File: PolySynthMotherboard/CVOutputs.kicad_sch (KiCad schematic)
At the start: 167 parts, among them U301 DAC7578xPW, U302 TL074, U303 TL072, U304 TMUX4051, U305 TL074, U306 TMUX4051, U307 TL074, U308 TMUX4051, U309 TMUX4051, U310 TL074, U311 TL074, U312 TL074, U313 TMUX4051, U314 TL074, U315 TL074, U316 TL074, U317 TMUX4051, U318 TMUX4051, U319 TL074, U320 TL074

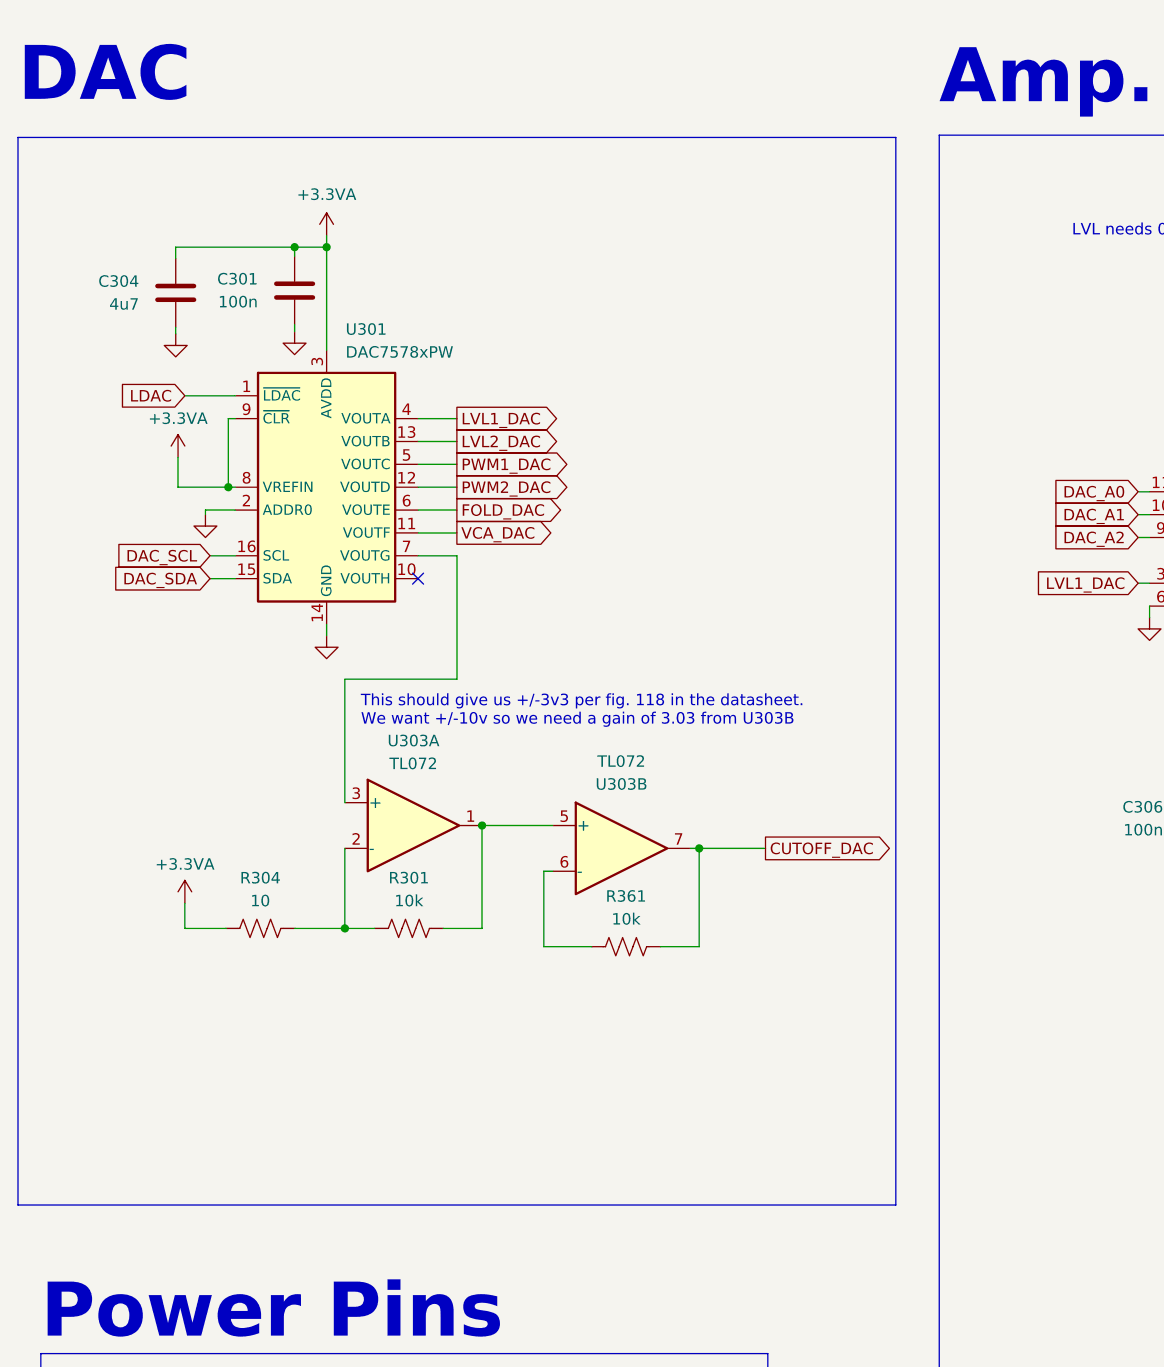
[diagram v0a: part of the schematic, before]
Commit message: DAC7578 driver
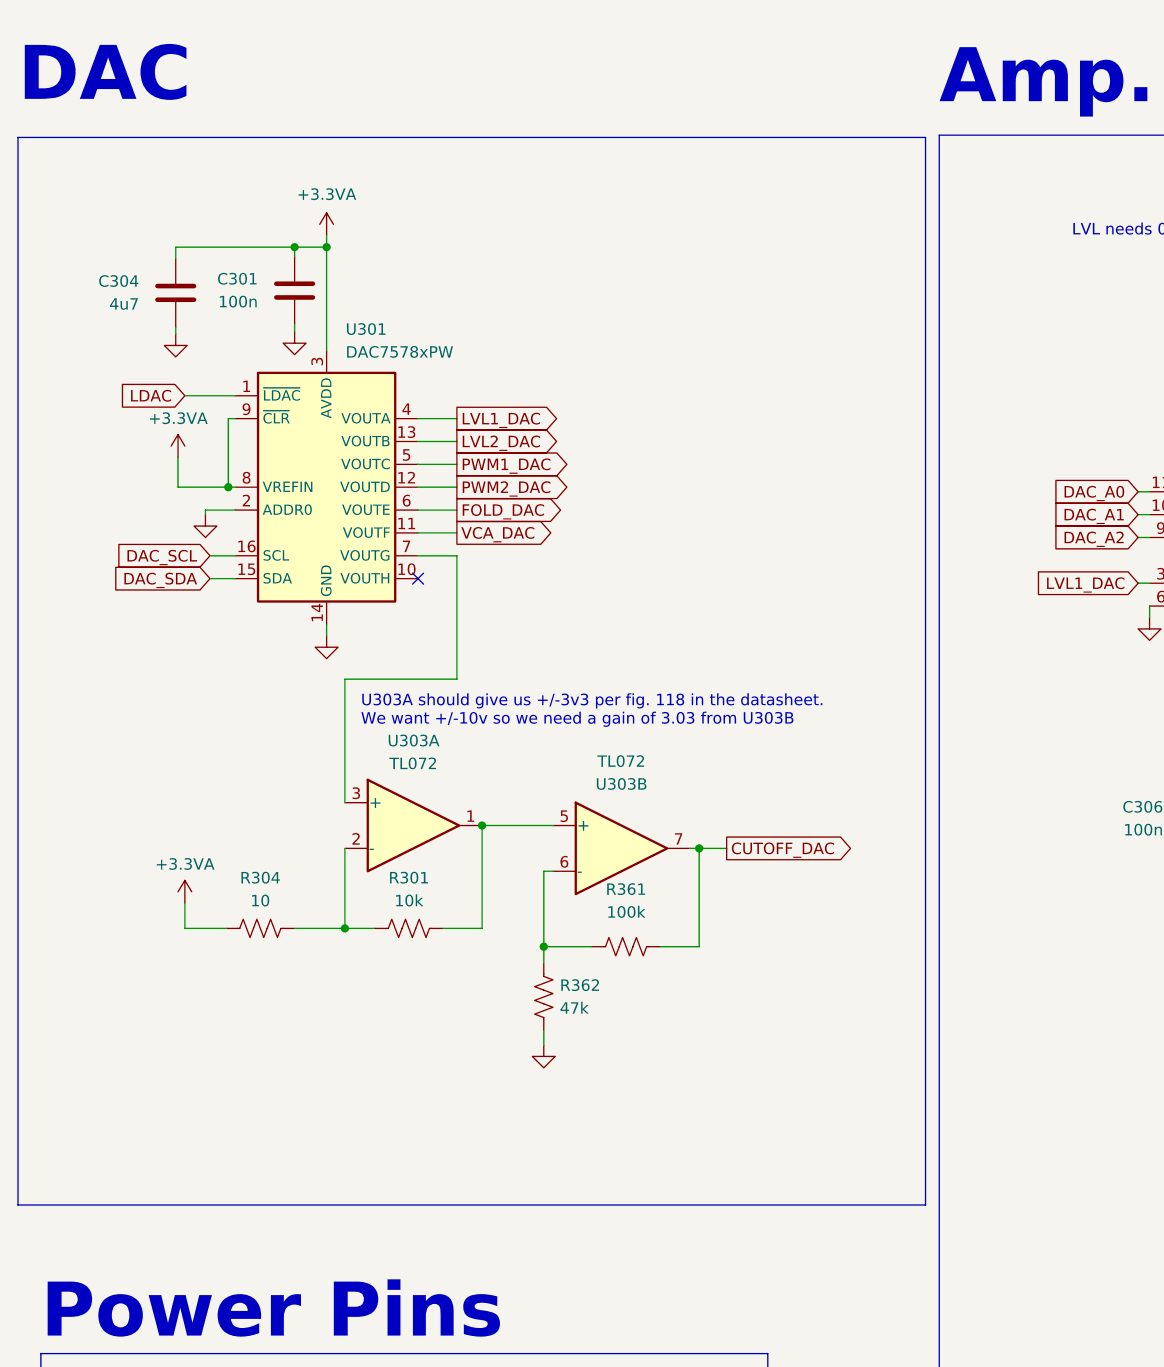
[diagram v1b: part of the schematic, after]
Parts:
- added R362: 47k, symbol Device:R_US
- R361: value 10k -> 100k
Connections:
- net GND: now also R362.1
- net at R361.1, U303.6 (-): now also R362.2
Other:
- note added: "U303A should give us +/-3v3 per fig. 118 in the datasheet. We want +/-10v so we need a gain of 3.03 from U303B"
- note removed: "This should give us +/-3v3 per fig. 118 in the datasheet. We want +/-10v so we need a gain of 3.03 from U303B"
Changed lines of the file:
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@@
   (junction (at 172.466 241.554) (diameter 0) (color 0 0 0 0)
   )
+  (junction (at 75.692 116.84) (diameter 0) (color 0 0 0 0)
+  )
   (junction (at 347.472 123.698) (diameter 0) (color 0 0 0 0)
   )
@@
     (stroke (width 0) (type default))
   )
+  (wire (pts (xy 75.692 116.84) (xy 75.692 118.618))
+    (stroke (width 0) (type default))
+  )
   (wire (pts (xy 48.006 114.808) (xy 53.594 114.808))
     (stroke (width 0) (type default))
@@
     (stroke (width 0) (type default))
   )
-  (wire (pts (xy 92.964 105.918) (xy 100.33 105.918))
+  (wire (pts (xy 92.964 105.918) (xy 96.012 105.918))
     (stroke (width 0) (type default))
   )
@@
     (stroke (width 0) (type default))
   )
+  (wire (pts (xy 75.692 126.238) (xy 75.692 127.762))
+    (stroke (width 0) (type default))
+  )
   (wire (pts (xy 45.72 372.11) (xy 45.72 381.254))
     (stroke (width 0) (type default))
@@
     (stroke (width 0) (type default))
   )
-  (rectangle (start 17.272 26.924) (end 114.808 145.542)
+  (rectangle (start 17.272 26.924) (end 118.11 145.542)
     (stroke (width 0) (type default))
     (fill (type none))
@@
     (effects (font (size 6 6) (thickness 3.6) bold) (justify left bottom))
   )
-  (text "This should give us +/-3v3 per fig. 118 in the datasheet.\nWe want +/-10v so we need a gain of 3.03 from U303B"
+  (text "U303A should give us +/-3v3 per fig. 118 in the datasheet.\nWe want +/-10v so we need a gain of 3.03 from U303B"
     (at 55.372 92.456 0)
     (effects (font (size 1.27 1.27)) (justify left bottom))
@@
     )
   )
-  (global_label "CUTOFF_DAC" (shape output) (at 100.33 105.918 0) (fields_autoplaced)
+  (global_label "CUTOFF_DAC" (shape output) (at 96.012 105.918 0) (fields_autoplaced)
     (effects (font (size 1.27 1.27)) (justify left))
-    (property "Intersheetrefs" "${INTERSHEET_REFS}" (at 114.9872 105.918 0)
+    (property "Intersheetrefs" "${INTERSHEET_REFS}" (at 110.6692 105.918 0)
       (effects (font (size 1.27 1.27)) (justify left) hide)
     )
@@
   (symbol (lib_id "Device:R_US") (at 84.836 116.84 90) (unit 1)
     (in_bom yes) (on_board yes) (dnp no) (fields_autoplaced)
-    (property "Reference" "R361" (at 84.836 111.252 90)
+    (property "Reference" "R361" (at 84.836 110.49 90)
       (effects (font (size 1.27 1.27)))
     )
-    (property "Value" "10k" (at 84.836 113.792 90)
+    (property "Value" "100k" (at 84.836 113.03 90)
       (effects (font (size 1.27 1.27)))
     )
@@
     )
   )
+  (symbol (lib_id "Device:R_US") (at 75.692 122.428 180) (unit 1)
+    (in_bom yes) (on_board yes) (dnp no) (fields_autoplaced)
+    (property "Reference" "R362" (at 77.47 121.158 0)
+      (effects (font (size 1.27 1.27)) (justify right))
+    )
+    (property "Value" "47k" (at 77.47 123.698 0)
+      (effects (font (size 1.27 1.27)) (justify right))
+    )
+    (property "Footprint" "" (at 74.676 122.174 90)
+      (effects (font (size 1.27 1.27)) hide)
+    )
+    (property "Datasheet" "~" (at 75.692 122.428 0)
+      (effects (font (size 1.27 1.27)) hide)
+    )
+    (pin "1")
+    (pin "2")
+    (instances
+      (project "PolySynthMotherboard"
+        (path "/22649217-9810-470f-bc7b-6f743ad2b90e/de3a0e63-5262-4eb9-b189-cca2b77e46b4"
+          (reference "R362") (unit 1)
+        )
+      )
+    )
+  )
   (symbol (lib_id "Device:C") (at 174.498 145.288 0) (unit 1)
     (in_bom yes) (on_board yes) (dnp no)
@@
         )
       )
+    )
+  )
+  (symbol (lib_id "power:GND") (at 75.692 127.762 0) (unit 1)
+    (in_bom yes) (on_board yes) (dnp no) (fields_autoplaced)
+    (property "Reference" "#PWR0469" (at 75.692 134.112 0)
+      (effects (font (size 1.27 1.27)) hide)
+    )
+    (property "Value" "GND" (at 75.692 131.572 0)
+      (effects (font (size 1.27 1.27)) hide)
+    )
+    (property "Footprint" "" (at 75.692 127.762 0)
+      (effects (font (size 1.27 1.27)) hide)
+    )
+    (property "Datasheet" "" (at 75.692 127.762 0)
+      (effects (font (size 1.27 1.27)) hide)
+    )
+    (pin "1")
+    (instances
+      (project "PolySynthMotherboard"
+        (path "/22649217-9810-470f-bc7b-6f743ad2b90e/de3a0e63-5262-4eb9-b189-cca2b77e46b4"
+          (reference "#PWR0469") (unit 1)
+        )
+      )

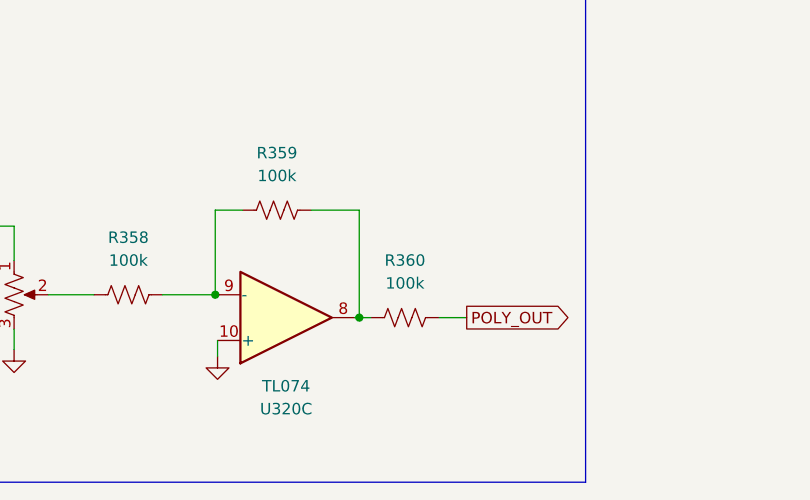
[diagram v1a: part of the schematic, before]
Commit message: ioc for standalone F411
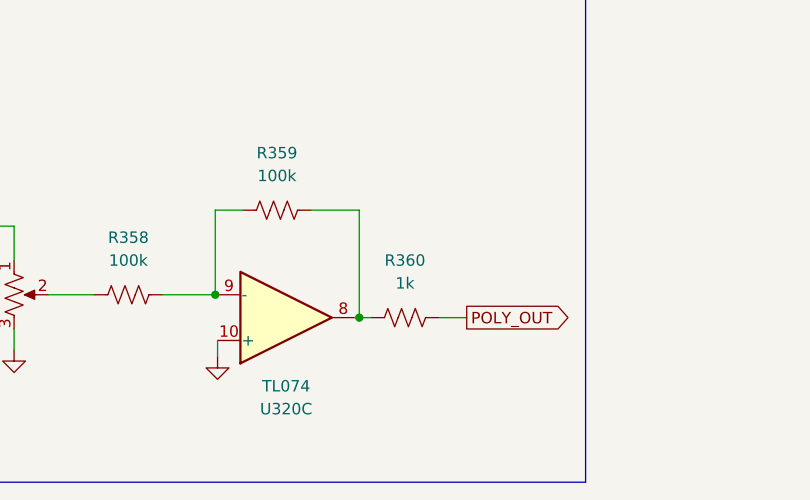
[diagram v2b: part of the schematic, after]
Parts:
- R360: value 100k -> 1k
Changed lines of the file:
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@@
       (effects (font (size 1.27 1.27)))
     )
-    (property "Value" "100k" (at 140.716 381 90)
+    (property "Value" "1k" (at 140.716 381 90)
       (effects (font (size 1.27 1.27)))
     )

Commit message: power supply/ output circuits
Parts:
- removed C383: 1u, symbol Device:C
- removed C384, C385: 100n, symbol Device:C
- removed R351, R352, R353, R354, R355, R356: 47k, symbol Device:R_US
- removed R357, R358, R359: 100k, symbol Device:R_US
- removed R360: 1k, symbol Device:R_US
- removed RV301: 100kA, symbol Device:R_Potentiometer_US
- removed U303: TL072, symbol Amplifier_Operational:TL072
- C301, C302, C303, C304, C305, C306, C307, C308, C309, C310, C311, C312, C313, C314, C315, C316, C317, C318, C319, C320, C321, C322, C323, C324, C325, C326, C327, C328, C329, C330, C331, C332, C333, C334, C335, C336, C337, C338, C339, C340, C341, C342, C343, C344, C345, C346, C347, C348, C349, C350, C351, C352, C353, C354, C355, C356, C357, C358, C359, C360, C361, C362, C363, C364, C365, C366, C367, C368, C369, C370, C371, C372, C373, C374, C375, C376, C377, C378, C379, C380, C381, C382: footprint (none) -> Capacitor_SMD:C_0805_2012Metric
- R301, R302, R303, R304, R305, R306, R307, R308, R309, R310, R311, R312, R313, R314, R315, R316, R317, R318, R319, R320, R321, R322, R323, R324, R325, R326, R327, R328, R329, R330, R331, R332, R333, R334, R335, R336, R337, R338, R339, R340, R341, R342, R343, R344, R345, R346, R347, R348, R349, R350, R361, R362: footprint (none) -> PCM_Resistor_SMD_AKL:R_0805_2012Metric
- U302, U305, U307, U310, U311, U312, U314, U315, U316, U319, U320: footprint (none) -> PCM_Package_SO_AKL:SOIC-14_3.9x8.7mm_P1.27mm
- U304, U306, U308, U309, U313, U317, U318: footprint (none) -> Package_SO:TSSOP-16_4.4x5mm_P0.65mm
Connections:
- net CUTOFF_DAC: now also U320.8
- net GND: no longer U320.10 (+), U320.12 (+)
- net at R301.2: now also U320.10 (+), U320.14
- net at R361.1, R362.2: now also U320.9 (-)
- net at U320.13 (-): now also R301.1, R304.2
- net at U301.7 (VOUTG): now also U320.12 (+)
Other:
- note removed: "Mixer & Audio Out"
- moved on the sheet: U320C, U320D

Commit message: board layout
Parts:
- removed C320, C341: 470n, Capacitor_SMD:C_0805_2012Metric, symbol Device:C
- removed U320: TL074, PCM_Package_SO_AKL:SOIC-14_3.9x8.7mm_P1.27mm, symbol Amplifier_Operational:TL074
- added C383, C384: 100n, Capacitor_SMD:C_0805_2012Metric, symbol Device:C
- added U303, U320: TL072, Package_SO:SOIC-8_3.9x4.9mm_P1.27mm, symbol Amplifier_Operational:TL072
- R304: value 10 -> 10k
- U302, U305, U307, U310, U311, U312, U314, U315, U316, U319: footprint PCM_Package_SO_AKL:SOIC-14_3.9x8.7mm_P1.27mm -> Package_SO:SOIC-14_3.9x8.7mm_P1.27mm
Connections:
- net +12V: now also C383.1, U303.8 (V+), U320.8 (V+)
- net -12V: now also C384.1, U303.4 (V-), U320.4 (V-)
- net CUTOFF_DAC: now also U320.7
- net GND: now also C383.2, C384.2
- net VCA_V5: now also U303.1, U303.2 (-)
- net VCA_V6: now also U303.6 (-), U303.7
- net at U301.7 (VOUTG): now also U320.3 (+)
- net at R301.1, R304.2: now also U320.2 (-)
- net at R301.2: now also U320.1, U320.5 (+)
- net at R361.1, R362.2: now also U320.6 (-)
- net at C373.1, U318.5 (X5): now also U303.5 (+)
- net at C375.1, U318.1 (X4): now also U303.3 (+)
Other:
- moved on the sheet: C379, C380, U319E

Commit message: new voice board proj
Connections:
- net +3.3VA: no longer U301.8 (VREFIN), U301.9 (~{CLR})
- new net +3.3V: U301.8 (VREFIN), U301.9 (~{CLR})
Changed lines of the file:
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@@
+    )
+  )
+  (symbol (lib_id "power:+3.3V") (at 35.052 62.484 0) (unit 1)
+    (in_bom yes) (on_board yes) (dnp no)
+    (property "Reference" "#PWR0301" (at 35.052 66.294 0)
+      (effects (font (size 1.27 1.27)) hide)
+    )
+    (property "Value" "+3.3V" (at 31.115 60.833 0)
+      (effects (font (size 1.27 1.27)))
+    )
+    (property "Footprint" "" (at 35.052 62.484 0)
+      (effects (font (size 1.27 1.27)) hide)
+    )
+    (property "Datasheet" "" (at 35.052 62.484 0)
+      (effects (font (size 1.27 1.27)) hide)
+    )
+    (pin "1")
+    (instances
+      (project "PolySynthMotherboard"
+        (path "/22649217-9810-470f-bc7b-6f743ad2b90e/de3a0e63-5262-4eb9-b189-cca2b77e46b4"
+          (reference "#PWR0301") (unit 1)
+        )
+      )
     )
   )
@@
     )
   )
-  (symbol (lib_id "power:+3.3VA") (at 35.052 62.484 0) (unit 1)
-    (in_bom yes) (on_board yes) (dnp no) (fields_autoplaced)
-    (property "Reference" "#PWR0310" (at 35.052 66.294 0)
-      (effects (font (size 1.27 1.27)) hide)
-    )
-    (property "Value" "+3.3VA" (at 35.052 58.166 0)
-      (effects (font (size 1.27 1.27)))
-    )
-    (property "Footprint" "" (at 35.052 62.484 0)
-      (effects (font (size 1.27 1.27)) hide)
-    )
-    (property "Datasheet" "" (at 35.052 62.484 0)
-      (effects (font (size 1.27 1.27)) hide)
-    )
-    (pin "1")
-    (instances
-      (project "PolySynthMotherboard"
-        (path "/22649217-9810-470f-bc7b-6f743ad2b90e/de3a0e63-5262-4eb9-b189-cca2b77e46b4"
-          (reference "#PWR0310") (unit 1)
-        )
-      )
-    )
-  )
   (symbol (lib_id "power:-12V") (at 32.766 229.362 180) (unit 1)
     (in_bom yes) (on_board yes) (dnp no) (fields_autoplaced)
@@
     )
   )
-  (symbol (lib_id "power:+3.3VA") (at 51.562 37.846 0) (unit 1)
-    (in_bom yes) (on_board yes) (dnp no) (fields_autoplaced)
-    (property "Reference" "#PWR0301" (at 51.562 41.656 0)
-      (effects (font (size 1.27 1.27)) hide)
-    )
-    (property "Value" "+3.3VA" (at 51.562 33.274 0)
-      (effects (font (size 1.27 1.27)))
-    )
-    (property "Footprint" "" (at 51.562 37.846 0)
-      (effects (font (size 1.27 1.27)) hide)
-    )
-    (property "Datasheet" "" (at 51.562 37.846 0)
-      (effects (font (size 1.27 1.27)) hide)
-    )
-    (pin "1")
-    (instances
-      (project "PolySynthMotherboard"
-        (path "/22649217-9810-470f-bc7b-6f743ad2b90e/de3a0e63-5262-4eb9-b189-cca2b77e46b4"
-          (reference "#PWR0301") (unit 1)
-        )
-      )
-    )
-  )
   (symbol (lib_id "Device:C") (at 303.022 289.052 0) (unit 1)
     (in_bom yes) (on_board yes) (dnp no)
@@
         )
       )
+    )
+  )
+  (symbol (lib_id "power:+3.3VA") (at 51.562 37.846 0) (unit 1)
+    (in_bom yes) (on_board yes) (dnp no) (fields_autoplaced)
+    (property "Reference" "#PWR0310" (at 51.562 41.656 0)
+      (effects (font (size 1.27 1.27)) hide)
+    )
+    (property "Value" "+3.3VA" (at 51.562 33.02 0)
+      (effects (font (size 1.27 1.27)))
+    )
+    (property "Footprint" "" (at 51.562 37.846 0)
+      (effects (font (size 1.27 1.27)) hide)
+    )
+    (property "Datasheet" "" (at 51.562 37.846 0)
+      (effects (font (size 1.27 1.27)) hide)
+    )
+    (pin "1")
+    (instances
+      (project "PolySynthMotherboard"
+        (path "/22649217-9810-470f-bc7b-6f743ad2b90e/de3a0e63-5262-4eb9-b189-cca2b77e46b4"
+          (reference "#PWR0310") (unit 1)
+        )
+      )
